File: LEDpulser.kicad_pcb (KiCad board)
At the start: 2 copper layers, 44.5 x 144.8 mm, 59 parts, among them J1 RJ45_Shielded, J2 0731375003, J3 0731375003, J4 Conn_01x04_Female, Q1 AO3401A, Q2 AO3400A, Q3 AO3400A, SW1 ATE1D-5M3-10-Z, U1 74HC123, U10 LT3082, U2 74HC123, U3 74HC123, U4 74HC10, U5 LT1121-5, U6 PM8834, U7 NE555, U8 PM8834, U9 PM8834

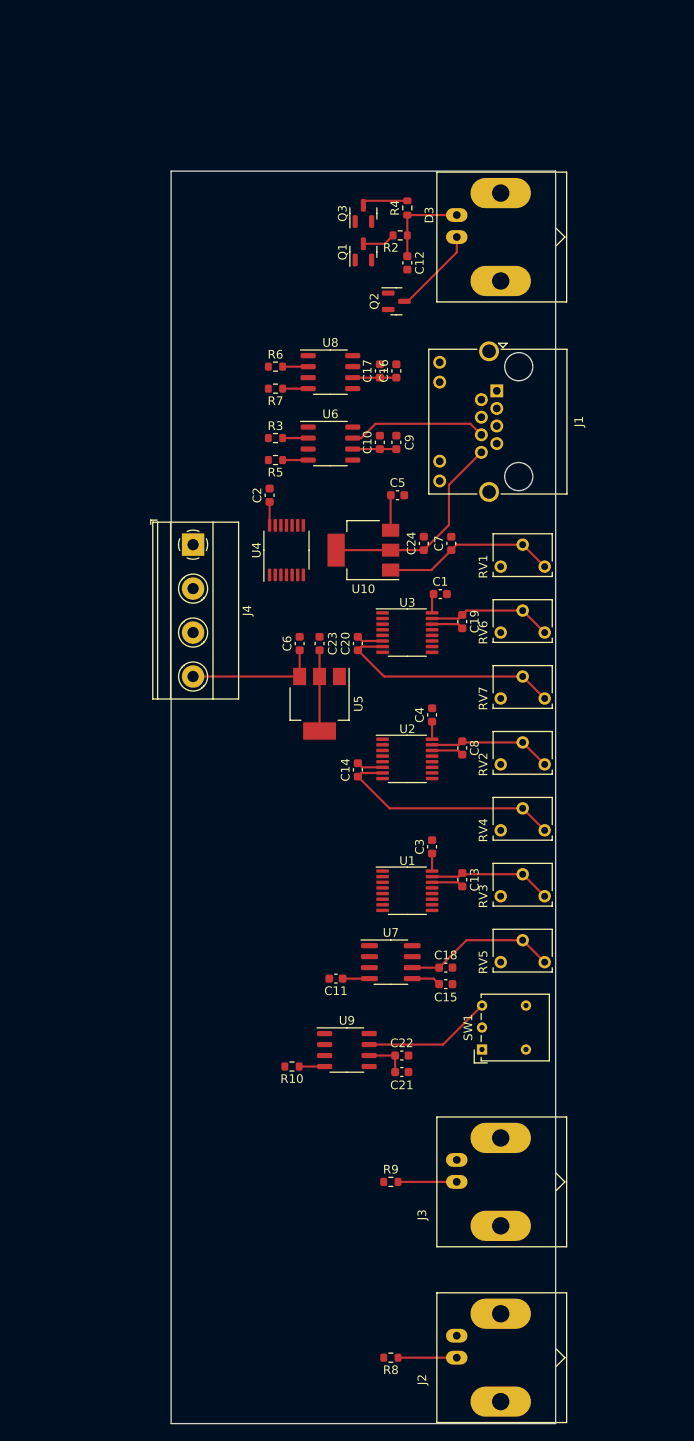
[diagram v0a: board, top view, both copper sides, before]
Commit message: Reducing board length.
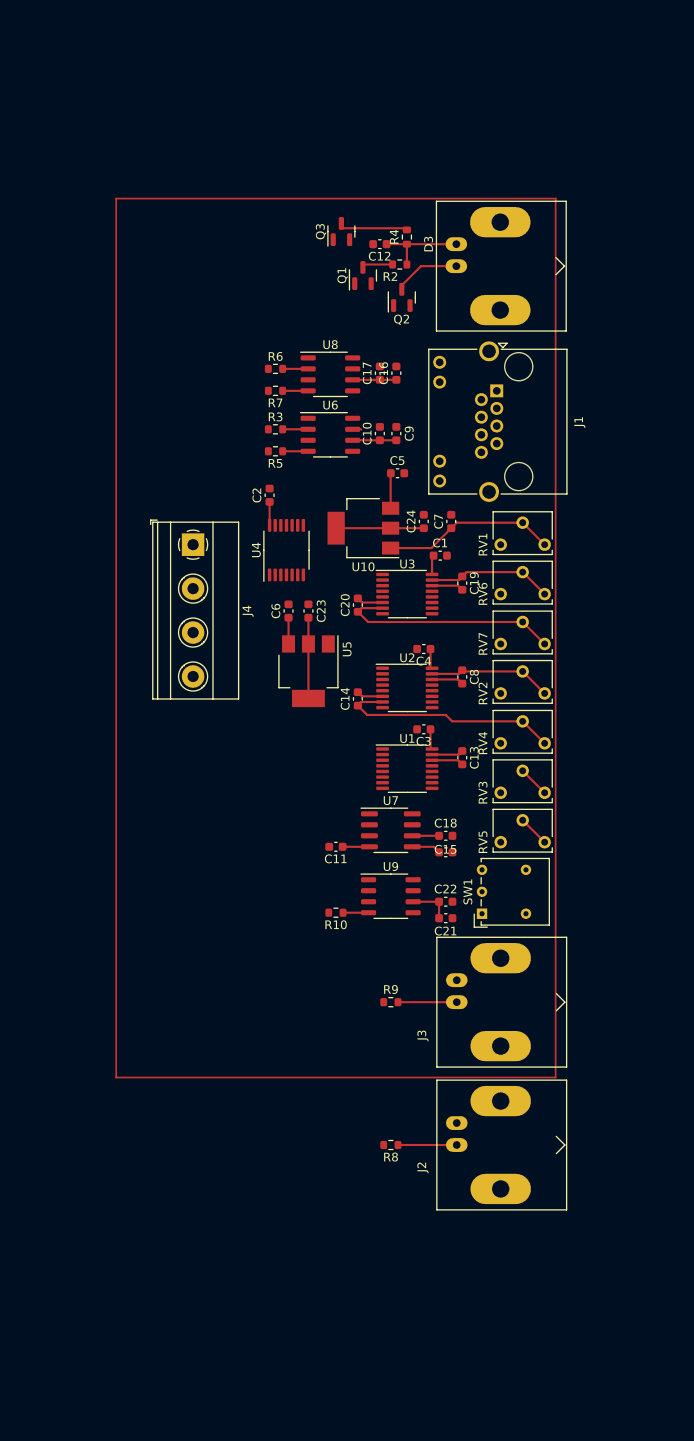
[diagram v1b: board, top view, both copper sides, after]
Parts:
- moved J2 24.6 mm to (127.0, 130.4)
- moved R8 24.6 mm to (119.4, 130.4)
- moved J3 20.8 mm to (127.0, 113.8)
- moved R9 20.8 mm to (119.4, 113.8)
- moved C21 18.5 mm to (125.7, 104.1)
- moved C22 18.5 mm to (125.7, 102.2)
- moved R10 18.5 mm to (113.0, 103.5)
- moved U9 18.5 mm to (119.4, 101.6)
- moved SW1 15.7 mm to (129.9, 103.6)
- moved C15 15.2 mm to (125.7, 96.5)
- moved C18 15.2 mm to (125.7, 94.6)
- moved C11 15.2 mm to (113.0, 95.9)
- moved U7 15.2 mm to (119.4, 94.0)
- moved C13 14.1 mm to (127.6, 85.6)
- moved U1 14.1 mm to (121.3, 86.9)
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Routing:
- net /CAP_CHARGE: track 16.1 -> 0.99 mm
- net Net-(SW1-Pad3): track 14.9 -> 0.00 mm
- net /CAP_VOLTAGE: track 24.2 -> 10.1 mm
- net +6V: track 15.4 -> 3.03 mm
- net Net-(C18-Pad1): track 17.7 -> 6.69 mm
- net Net-(C13-Pad1): track 14.3 -> 7.45 mm
- net Net-(D3-Pad1): track 10.8 -> 7.68 mm
- net Net-(Q3-Pad3): track 5.49 -> 8.53 mm
- net Net-(C20-Pad1): track 26.9 -> 26.2 mm
- net Net-(C14-Pad1): track 27.2 -> 26.4 mm
- net +5V: track 31.4 -> 32.2 mm
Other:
- board outline removed

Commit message: Routed first draft
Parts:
- removed D3: LED, Connector_Coaxial:BNC_Amphenol_B6252HB-NPP3G-50_Horizontal
- added H1: MountingHole, MountingHole:MountingHole_3.2mm_M3, F.Cu at (105.3, 29.3)
- added H2: MountingHole, MountingHole:MountingHole_3.2mm_M3, F.Cu at (105.3, 119.5)
- added J5: LED, Connector:FanPinHeader_1x03_P2.54mm_Vertical, F.Cu at (132.5, 31.2)
- C13: value 330pF -> C
- J2, J3: value 0731375003 -> EPS.00.250.NTN; footprint Connector_Coaxial:BNC_Amphenol_B6252HB-NPP3G-50_Horizontal -> Connector_Coaxial:SMA_Amphenol_132203-12_Horizontal
- R4: value 100 -> 50
- RV1: footprint Potentiometer_THT:Potentiometer_Vishay_T73XX_Horizontal -> Potentiometer_THT:Potentiometer_Bourns_3266X_Horizontal
- RV2, RV3, RV4, RV6, RV7: value 1k -> 2k; footprint Potentiometer_THT:Potentiometer_Vishay_T73XX_Horizontal -> Potentiometer_THT:Potentiometer_Bourns_3266X_Horizontal
- RV5: value 1k -> 1M; footprint Potentiometer_THT:Potentiometer_Vishay_T73XX_Horizontal -> Potentiometer_THT:Potentiometer_Bourns_3266X_Horizontal
- moved C14 15.8 mm to (128.7, 87.7), turned to 180 degrees
- moved J4 15.2 mm to (106.1, 72.8)
- moved C20 13.9 mm to (128.7, 72.8), turned to 180 degrees
- moved R8 11.4 mm to (122.3, 119.4)
- moved J2 11.4 mm to (129.9, 119.4)
- moved C3 11.2 mm to (122.2, 93.5), turned to 90 degrees
- moved U1 11.2 mm to (126.2, 96.9), turned to 90 degrees
- moved C23 9.17 mm to (117.2, 74.1)
- moved C6 9.17 mm to (114.9, 74.1)
- moved U5 9.17 mm to (117.2, 81.1)
- moved U2 8.44 mm to (128.0, 82.6), turned to 90 degrees
- moved C15 8.12 mm to (117.7, 97.9)
- moved C18 8.12 mm to (117.7, 96.0)
- moved C21 8.07 mm to (117.7, 105.2)
- moved C22 8.07 mm to (117.7, 103.3)
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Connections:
- Q2 pad 1: /LED_ON -> unconnected-(Q2-Pad1)
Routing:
- net GND: track 0.00 -> 410.9 mm
- net +5V: track 32.2 -> 207.9 mm
- net /CAP_VOLTAGE: track 10.1 -> 65.7 mm
- net Net-(R6-Pad1): track 2.95 -> 56.3 mm, vias 0 -> 2
- net Net-(R10-Pad1): track 2.95 -> 55.6 mm, vias 0 -> 4
- net Net-(U2-Pad4): track 0.00 -> 36.5 mm
- net /LED_SHORT: track 0.00 -> 36.5 mm
- net Net-(R7-Pad1): track 2.95 -> 38.5 mm, vias 0 -> 2
- net /INT: track 0.00 -> 33.7 mm, vias 0 -> 1
- net Net-(U2-Pad12): track 0.00 -> 31.4 mm, vias 0 -> 2
- net +12V: track 9.11 -> 39.5 mm, vias 0 -> 1
- net /CAP_CHARGE: track 0.99 -> 29.7 mm, vias 0 -> 1
- net Net-(C18-Pad1): track 6.69 -> 34.2 mm
- net /EXT: track 6.80 -> 30.6 mm
- net Net-(U3-Pad12): track 0.00 -> 23.5 mm, vias 0 -> 2
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- added copper zone on B.Cu, net GND
- added copper zone on F.Cu, net GND
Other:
- board outline added: 38.2 x 98.2 mm

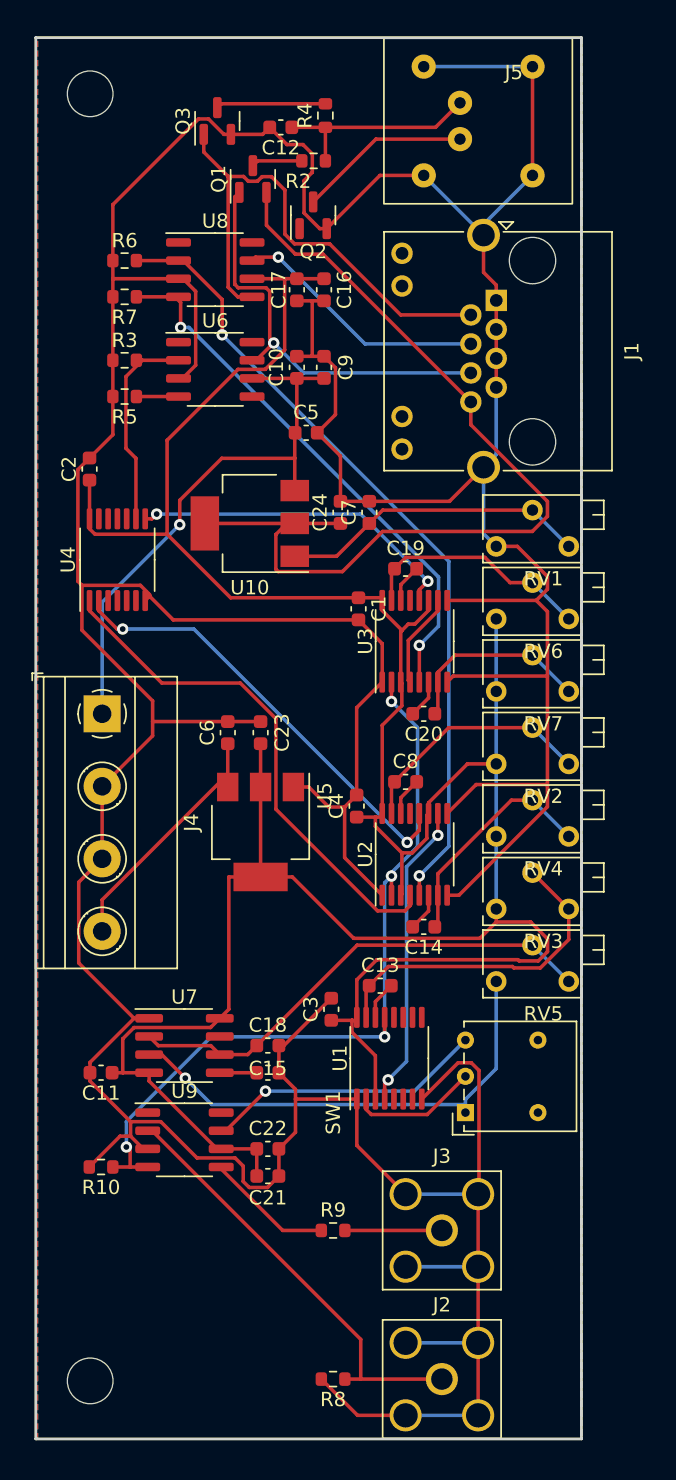
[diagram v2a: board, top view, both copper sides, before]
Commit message: Changed switch, added sync pulse monostable, rerouted.
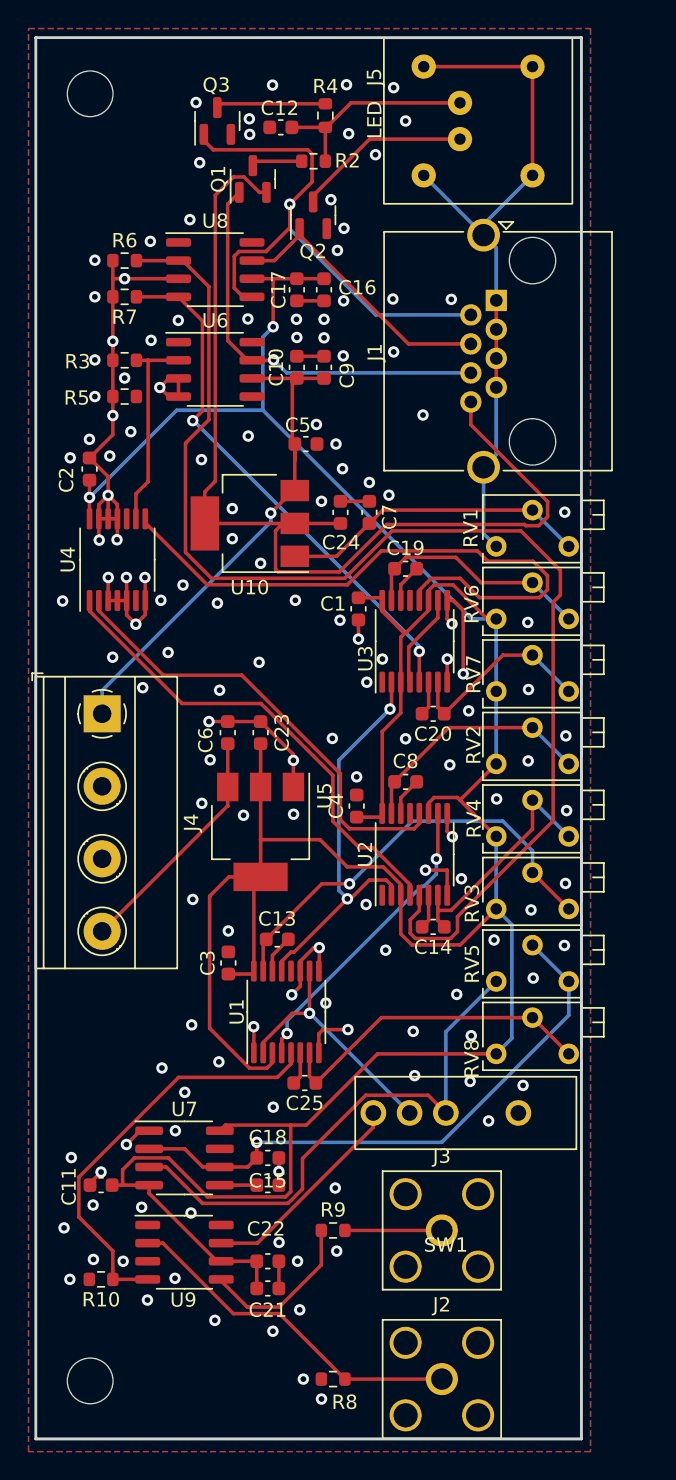
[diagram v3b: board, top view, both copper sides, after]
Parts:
- added C25: C, Capacitor_SMD:C_0603_1608Metric, F.Cu at (120.3, 98.6)
- added RV8: 2k, Potentiometer_THT:Potentiometer_Bourns_3266X_Horizontal, F.Cu at (133.7, 96.6)
- J1: value RJ45_Shielded -> RJHSE5380; footprint Connector_RJ:RJ45_Amphenol_RJHSE538X -> Connector_RJ:RJ45_Amphenol_RJHSE5380
- R8: value 50 -> 100k
- SW1: value ATE1D-5M3-10-Z -> BST11T2AVR
- moved C3 7.91 mm to (115.0, 90.2)
- moved C13 7.91 mm to (118.4, 88.6)
- moved U1 7.91 mm to (119.0, 93.7)
- moved C11 7.87 mm to (106.0, 105.8)
- moved C15 7.87 mm to (117.7, 105.8)
- moved C18 7.87 mm to (117.7, 103.9)
- moved C21 7.87 mm to (117.7, 113.0)
- moved C22 7.87 mm to (117.7, 111.1)
- moved R10 7.87 mm to (106.0, 112.4)
- moved U7 7.87 mm to (111.9, 103.9)
- moved U9 7.87 mm to (111.9, 110.5)
- moved SW1 1.37 mm to (130.2, 100.7), turned to 180 degrees
- moved C5 0.79 mm to (120.4, 53.9)
- moved C14 0.66 mm to (129.3, 87.7)
- moved C20 0.66 mm to (129.3, 72.8)
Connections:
- Q2 pad 1: unconnected-(Q2-Pad1) -> /LED_ON
- U1 pad 10: (no net) -> Net-(SW1-Pad2)
- U1 pad 11: (no net) -> GND
- U1 pad 12: (no net) -> unconnected-(U1-Pad12)
- U1 pad 13: Net-(R10-Pad1) -> Net-(U1-Pad13)
- U1 pad 5: (no net) -> Net-(R10-Pad1)
- U1 pad 6: (no net) -> Net-(C25-Pad2)
- U1 pad 7: (no net) -> Net-(C25-Pad1)
- U1 pad 9: (no net) -> GND
- U2 pad 2: Net-(R10-Pad1) -> Net-(U1-Pad13)
- U3 pad 2: Net-(R10-Pad1) -> Net-(U1-Pad13)
- U4 pad 10: (no net) -> unconnected-(U4-Pad10)
- U4 pad 11: (no net) -> GND
- U4 pad 12: (no net) -> GND
- U4 pad 13: (no net) -> GND
- U4 pad 3: (no net) -> GND
- U4 pad 4: (no net) -> GND
- U4 pad 5: (no net) -> GND
- U4 pad 6: (no net) -> unconnected-(U4-Pad6)
- U6 pad 4: Net-(R5-Pad1) -> GND
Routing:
- net GND: track 410.9 -> 145.5 mm, vias 0 -> 146
- net Net-(R6-Pad1): track 56.3 -> 89.5 mm, vias 2 -> 0
- net +5V: track 207.9 -> 236.6 mm, vias 0 -> 2
- net Net-(U1-Pad13): track 0.00 -> 28.5 mm, vias 0 -> 2
- net Net-(R10-Pad1): track 55.6 -> 29.5 mm, vias 4 -> 0
- net Net-(C25-Pad1): track 0.00 -> 23.4 mm
- net Net-(U3-Pad12): track 23.5 -> 43.8 mm, vias 2 -> 0
- net Net-(SW1-Pad2): track 8.94 -> 17.7 mm, vias 0 -> 1
- net Net-(C13-Pad1): track 23.4 -> 30.4 mm, vias 0 -> 1
- net Net-(C18-Pad1): track 34.2 -> 40.9 mm, vias 0 -> 1
- net /CAP_VOLTAGE: track 65.7 -> 71.9 mm
- net /EXT: track 30.6 -> 24.6 mm
- net Net-(SW1-Pad3): track 19.7 -> 15.0 mm, vias 1 -> 0
- net +12V: track 39.5 -> 35.4 mm
- net /INT: track 33.7 -> 37.4 mm, vias 1 -> 0
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
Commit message: reverted to previous commit
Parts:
- removed C25: C, Capacitor_SMD:C_0603_1608Metric
- removed RV8: 2k, Potentiometer_THT:Potentiometer_Bourns_3266X_Horizontal
- J1: value RJHSE5380 -> RJ45_Shielded; footprint Connector_RJ:RJ45_Amphenol_RJHSE5380 -> Connector_RJ:RJ45_Amphenol_RJHSE538X
- R8: value 100k -> 50
- SW1: value BST11T2AVR -> ATE1D-5M3-10-Z
- moved C3 7.91 mm to (122.2, 93.5)
- moved C13 7.91 mm to (125.6, 91.8)
- moved U1 7.91 mm to (126.2, 96.9)
- moved C11 7.87 mm to (106.0, 97.9)
- moved C15 7.87 mm to (117.7, 97.9)
- moved C18 7.87 mm to (117.7, 96.0)
- moved C21 7.87 mm to (117.7, 105.2)
- moved C22 7.87 mm to (117.7, 103.3)
- moved R10 7.87 mm to (106.0, 104.5)
- moved U7 7.87 mm to (111.9, 96.0)
- moved U9 7.87 mm to (111.9, 102.6)
- moved SW1 1.37 mm to (131.6, 100.7), turned to 90 degrees
- moved C5 0.79 mm to (120.4, 53.1)
- moved C14 0.66 mm to (128.7, 87.7)
- moved C20 0.66 mm to (128.7, 72.8)
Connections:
- Q2 pad 1: /LED_ON -> unconnected-(Q2-Pad1)
- U1 pad 10: Net-(SW1-Pad2) -> (no net)
- U1 pad 11: GND -> (no net)
- U1 pad 12: unconnected-(U1-Pad12) -> (no net)
- U1 pad 13: Net-(U1-Pad13) -> Net-(R10-Pad1)
- U1 pad 5: Net-(R10-Pad1) -> (no net)
- U1 pad 6: Net-(C25-Pad2) -> (no net)
- U1 pad 7: Net-(C25-Pad1) -> (no net)
- U1 pad 9: GND -> (no net)
- U2 pad 2: Net-(U1-Pad13) -> Net-(R10-Pad1)
- U3 pad 2: Net-(U1-Pad13) -> Net-(R10-Pad1)
- U4 pad 10: unconnected-(U4-Pad10) -> (no net)
- U4 pad 11: GND -> (no net)
- U4 pad 12: GND -> (no net)
- U4 pad 13: GND -> (no net)
- U4 pad 3: GND -> (no net)
- U4 pad 4: GND -> (no net)
- U4 pad 5: GND -> (no net)
- U4 pad 6: unconnected-(U4-Pad6) -> (no net)
- U6 pad 4: GND -> Net-(R5-Pad1)
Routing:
- net GND: track 145.5 -> 410.9 mm, vias 146 -> 0
- net Net-(R6-Pad1): track 89.5 -> 56.3 mm, vias 0 -> 2
- net +5V: track 236.6 -> 207.9 mm, vias 2 -> 0
- net Net-(U1-Pad13): track 28.5 -> 0.00 mm, vias 2 -> 0
- net Net-(R10-Pad1): track 29.5 -> 55.6 mm, vias 0 -> 4
- net Net-(C25-Pad1): track 23.4 -> 0.00 mm
- net Net-(U3-Pad12): track 43.8 -> 23.5 mm, vias 0 -> 2
- net Net-(SW1-Pad2): track 17.7 -> 8.94 mm, vias 1 -> 0
- net Net-(C13-Pad1): track 30.4 -> 23.4 mm, vias 1 -> 0
- net Net-(C18-Pad1): track 40.9 -> 34.2 mm, vias 1 -> 0
- net /CAP_VOLTAGE: track 71.9 -> 65.7 mm
- net /EXT: track 24.6 -> 30.6 mm
- net Net-(SW1-Pad3): track 15.0 -> 19.7 mm, vias 0 -> 1
- net +12V: track 35.4 -> 39.5 mm
- net /INT: track 37.4 -> 33.7 mm, vias 0 -> 1
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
